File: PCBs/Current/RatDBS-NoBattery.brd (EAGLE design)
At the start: 55.9 x 19.1 mm, 41 parts

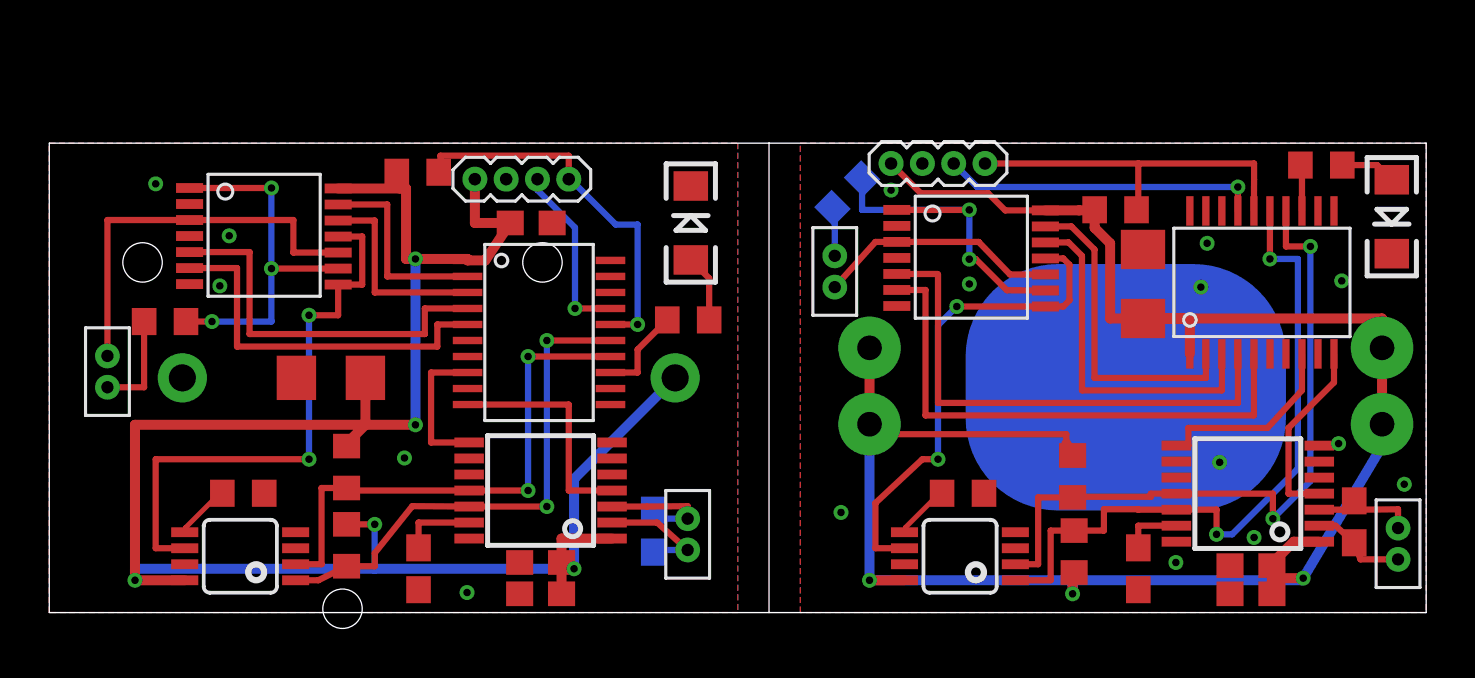
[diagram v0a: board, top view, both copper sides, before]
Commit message: Updated primary design and added two component (battery-on-separate-pcb) version)
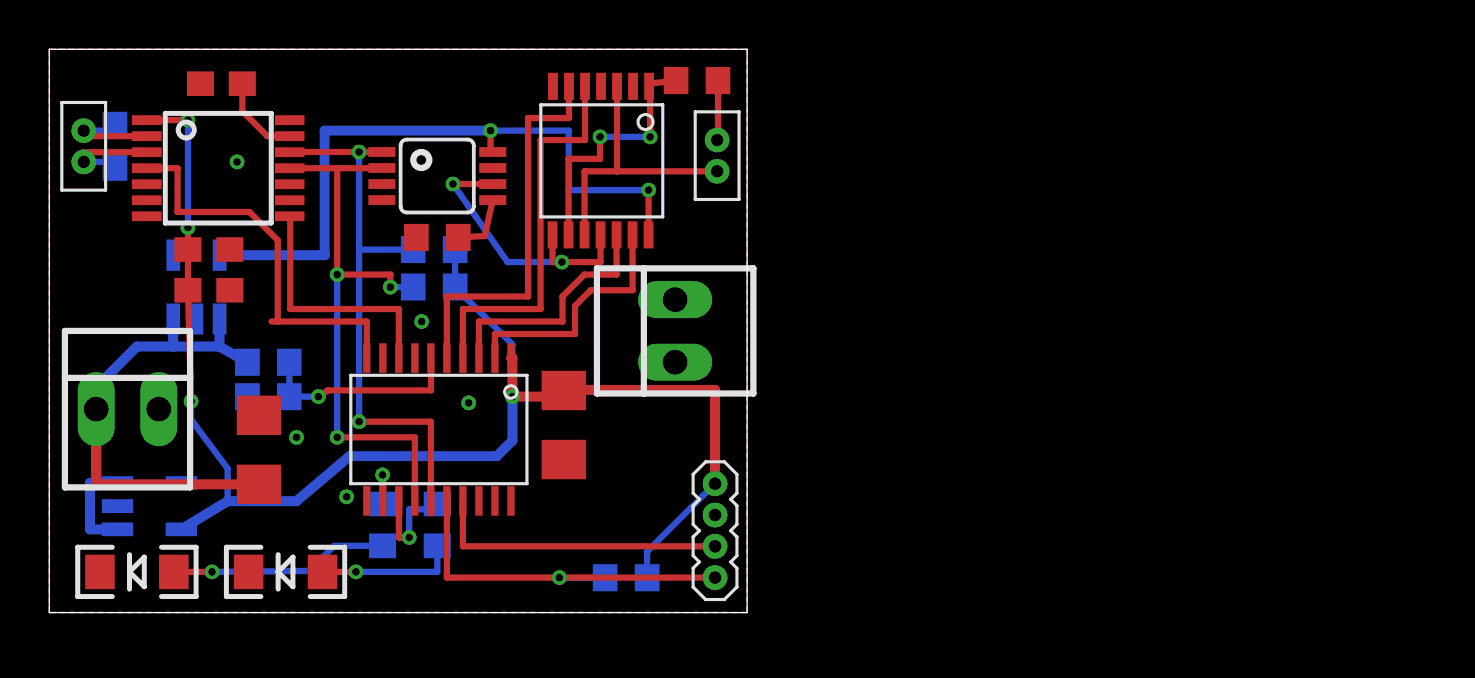
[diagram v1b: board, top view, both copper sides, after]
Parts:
- removed ANT1, STIM1: FTSH-102, Samtec50Mil:FTSH-102-DH
- removed BAT1: 20mm coincell, Battery:BATTCOM_20MM_PLASTIC_STUDS
- removed BAT2: 20mm coincell, Battery:BATTCON_20MM_PTH_COMPACT
- removed C5: 1µ, rcl:C0603
- removed CANT1: (no value), rcl:C0603
- removed CBAT: 10µ, rcl:C0603
- removed CBAT1: 10µ, rcl:C1206
- removed C_VC1: 0.47µ, rcl:C0603
- removed DS4432U+1: (no value), RatDBS:8_PIN
- removed JP2: (no value), SparkFun:1X04-1.27MM
- removed MSP1: MSP, RatDBS:20_PIN
- removed R1_I2C1, R2_I2C1, R_LOAD_EX1: 10k, BiphasicBoard:R0603
- removed R_INPUT_FS1: 47k, BiphasicBoard:R0603
- removed R_PULLUP_RST1: 43k, BiphasicBoard:R0603
- removed TS3A4751_1: SW, BiphasicBoard:14_PIN
- removed U$2: RF, RF430CL330H:PW_R-PDSO-G14
- added RDIV_1: RDIV_HIGH, BiphasicBoard:R0603
- added RDIV_2: RDIV_LOW, BiphasicBoard:R0603
- added U1: 3V, Texas Instruments_By_element14_Batch_1:SOT95P280X145-5N
- added U2: 5V, Texas Instruments_By_element14_Batch_1:SOT95P280X145-5N
- added X1, X2: 22-23-2021, con-molex:22-23-2021
- C1: value 1µ -> 1u
- C2: value 0.1µ -> 0.1u
- C3: value 100µ -> 100u
- C4: value 0.1µ -> 10u; device rcl:C0603 -> rcl:C1206
- CANT: value (none) -> C_NFC
- LED6: value GREEN -> RED
- R_LED: value R_LED -> R_LEDR
- R_LED1: value R_LED -> R_LEDG
- U$1: value RF -> NFC
- moved LED1 52.9 mm to (3.56, 1.65), turned to 180 degrees
- moved R_LED1 40.8 mm to (13.5, 3.56), flipped to the bottom, turned to 270 degrees
- moved ANT 29.1 mm to (1.40, 18.9), turned to 90 degrees
- moved C4 28.7 mm to (20.9, 7.61), turned to 270 degrees
- moved CANT 26.9 mm to (2.67, 18.9), turned to 90 degrees
- moved STIM 26.2 mm to (27.1, 18.5), turned to 90 degrees
- moved R_LOAD_EX 23.7 mm to (26.3, 21.6), turned to 180 degrees
- moved LED6 21.7 mm to (9.59, 1.65), turned to 180 degrees
- moved C_VC 21.2 mm to (6.99, 21.5), turned to 180 degrees
- moved C2 19.4 mm to (6.48, 14.7), turned to 0 degrees
- moved R_PULLUP_RST 18.5 mm to (23.4, 1.41), flipped to the bottom
- moved U$1 18.5 mm to (6.86, 18.0), turned to 270 degrees
- moved C1 17.4 mm to (6.48, 13.1), turned to 0 degrees
- moved DS4432U+ 17.4 mm to (15.7, 17.7), turned to 0 degrees
- moved JP1 15.7 mm to (27.0, 5.23), turned to 270 degrees
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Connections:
- removed net GND1: BAT2.2, C4.2, C5.2, CBAT1.1, C_VC1.2, DS4432U+1.4, JP2.2, LED1.C, MSP1.20, R_INPUT_FS1.1, TS3A4751_1.2, TS3A4751_1.4, TS3A4751_1.7, U$2.10, U$2.14, U$2.5, U$2.6, U$2.7, U$2.9
- removed net IN5: MSP1.5, TS3A4751_1.6
- removed net IN6: MSP1.2, TS3A4751_1.13
- removed net IN7: MSP1.4, TS3A4751_1.5
- removed net IN8: MSP1.3, TS3A4751_1.12
- removed net N$13 (its old number): R_LOAD_EX1.1, STIM1.P$2
- removed net N$14: MSP1.7
- removed net N$15: C_VC1.1, U$2.13
- removed net N$16: ANT1.P$2, CANT1.2, U$2.2
- removed net N$17: ANT1.P$1, CANT1.1, U$2.3
- removed net N$18: MSP1.8, U$2.8
- removed net N$19: MSP1.10, U$2.4
- removed net SCL1: DS4432U+1.2, MSP1.14, R2_I2C1.1, U$2.11
- removed net SDA1: DS4432U+1.1, MSP1.15, R1_I2C1.1, U$2.12
- removed net STIM_IN1: DS4432U+1.6, TS3A4751_1.11, TS3A4751_1.8
- removed net STIM_OUT3: STIM1.P$1, TS3A4751_1.10, TS3A4751_1.3
- removed net STIM_OUT4: R_LOAD_EX1.2, TS3A4751_1.1, TS3A4751_1.9
- removed net TEST1: JP2.3, MSP1.17
- removed net VDD1: BAT2.1, BAT2.3, BAT2.4, BAT2.5, C4.1, C5.1, CBAT1.2, DS4432U+1.8, JP2.1, MSP1.1, R1_I2C1.2, R2_I2C1.2, R_PULLUP_RST1.2, TS3A4751_1.14, U$2.1
- removed net _RST1: JP2.4, MSP1.16, R_PULLUP_RST1.1
- new net BATIN: C3.1, RDIV_1.1, U1.1, U1.3, U2.1, U2.3, X1.1
- new net VDD5: DS4432U+.8, TS3A4751_0.14, U2.5
- net GND: now also C4.2, LED1.C, RDIV_2.1, U1.2, U2.2, X1.2; no longer BAT1.2, CBAT.1
- net N$10: now also MSP430.6, RDIV_1.2, RDIV_2.2; no longer DS4432U+1.5, R_INPUT_FS1.2
- net N$11: now also MSP430.12; no longer MSP1.13
- net VDD: now also C4.1, U1.5; no longer BAT1.1, C3.1, CBAT.2, DS4432U+.8, TS3A4751_0.14
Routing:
- net VDD1: track 84.3 -> 0.00 mm, vias 3 -> 0
- net SCL1: track 28.4 -> 0.00 mm, vias 2 -> 0
- net SDA1: track 28.1 -> 0.00 mm, vias 2 -> 0
- net VDD5: track 0.00 -> 27.7 mm, vias 0 -> 2
- net BATIN: track 0.00 -> 26.9 mm
- net IN5: track 22.1 -> 0.00 mm
- net IN7: track 21.0 -> 0.00 mm
- net VDD: track 80.0 -> 59.9 mm, vias 5 -> 4
- net STIM_IN1: track 20.0 -> 0.00 mm, vias 2 -> 0
- net _RST1: track 15.0 -> 0.00 mm
- net IN8: track 14.3 -> 0.00 mm
- net STIM_OUT4: track 14.2 -> 0.00 mm, vias 2 -> 0
- net IN6: track 13.1 -> 0.00 mm
- net TEST1: track 12.9 -> 0.00 mm, vias 1 -> 0
- net STIM_IN: track 23.2 -> 11.9 mm
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- removed copper zone on layer 1, net GND1
- removed copper zone on layer 16, net GND1
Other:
- board size 55.9 x 19.1 mm -> 28.3 x 22.9 mm
- board text added: "+ -"
- board text added: "5V"
- board text added: "NFC-RDBS Kemere Lab v3.0NB (C)2017"
- board text added: "RTGV"
- board text removed: "NFC-RDBS v1.2 Kemere Lab (C)2015"
- board text removed: "NFC-RDBS v1.2b Kemere Lab (C)2015"
- board text removed: "VGTR"
